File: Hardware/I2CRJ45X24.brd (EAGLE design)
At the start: 216 x 50 mm, 97 parts, among them IC1 MCP23017SO, IC2 MCP23017SO, IC3 MCP23017SO, IC4 MCP23017SO, IC5 MCP23017SO, IC6 MCP23017SO, J1 I2C-BREAKOUT, J2 I2C-BREAKOUT, J3 M01-PLAIN, J4 RJ45-X8, J5 RJ45-X8, J6 RJ45-X8

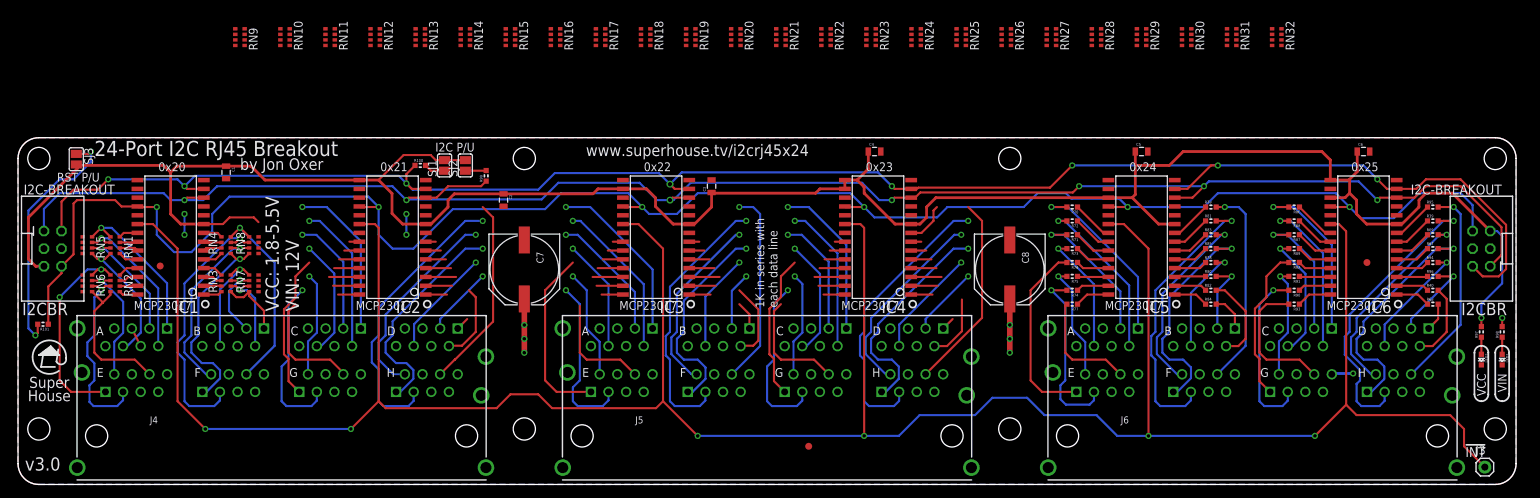
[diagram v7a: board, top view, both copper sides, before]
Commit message: Replace discrete resistors with resistor networks. Add hardware pull-ups to all input lines. Routing, ERC, and DRC for v3.0 release.
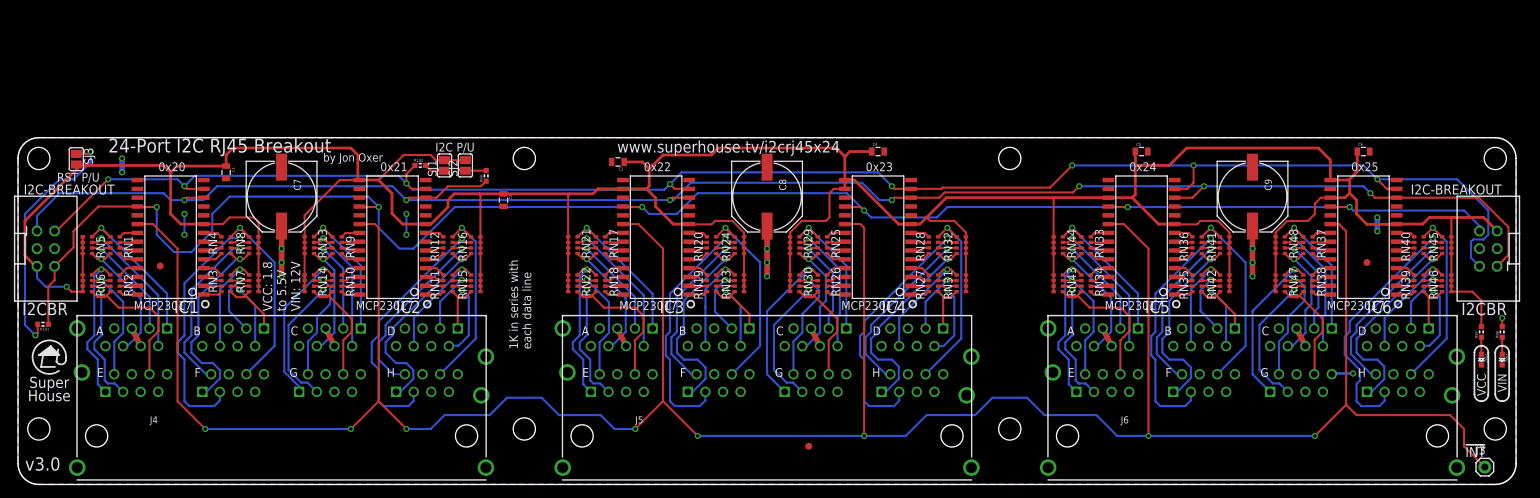
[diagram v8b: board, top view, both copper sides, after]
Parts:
- removed R39, R40, R67, R68, R69, R70, R71, R72, R73, R74, R75, R76, R77, R78, R79, R80, R81, R82, R83, R84, R85, R86, R87, R88, R89, R90, R91, R92, R93, R94, R95, R96: 1K, SuperHouse-DiscreteSemi:R0603
- added C9: 330uF 50V, SuperHouse-Capacitors:PANASONIC_G
- added RN33, RN34, RN35, RN36, RN37, RN38, RN39, RN40: 1K, SuperHouse-Resistors:CAY16
- added RN41, RN42, RN43, RN44, RN45, RN46, RN47, RN48: 10K, SuperHouse-Resistors:CAY16
- C1, C2, C3, C4, C5, C6: device SuperHouse-DiscreteSemi:C0805 -> SuperHouse-Capacitors:C0805
- C7, C8: device SuperHouse-DiscreteSemi:PANASONIC_G -> SuperHouse-Capacitors:PANASONIC_G
- R100, R101, R97, R98, R99: device SuperHouse-DiscreteSemi:R0603 -> SuperHouse-Resistors:R0603
- RN1, RN10, RN11, RN12, RN13, RN14, RN15, RN16, RN17, RN18, RN19, RN2, RN20, RN21, RN22, RN23, RN24, RN25, RN26, RN27, RN28, RN29, RN3, RN30, RN31, RN32, RN4, RN5, RN6, RN7, RN8, RN9: device SuperHouse-DiscreteSemi:CAY16 -> SuperHouse-Resistors:CAY16
- moved RN30 66.7 mm to (112.0, 29.0)
- moved RN29 58.3 mm to (112.0, 34.5)
- moved RN32 54.5 mm to (136.0, 34.5), turned to 270 degrees
- moved RN31 52.7 mm to (136.0, 29.0), turned to 270 degrees
- moved RN22 50.9 mm to (80.0, 29.0)
- moved RN26 44.3 mm to (116.0, 29.0)
- moved RN21 42.4 mm to (80.0, 34.5)
- moved RN14 42.0 mm to (42.0, 29.0)
- moved RN23 40.3 mm to (104.0, 29.0), turned to 270 degrees
- moved RN24 39.4 mm to (104.0, 34.5), turned to 270 degrees
- moved RN11 39.4 mm to (62.0, 29.0), turned to 270 degrees
- moved RN27 39.4 mm to (132.0, 29.0), turned to 270 degrees
- moved RN28 38.1 mm to (132.0, 34.5), turned to 270 degrees
- moved C7 36.5 mm to (38.0, 41.5)
- moved C8 36.5 mm to (108.0, 41.5)
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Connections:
- net 3A1: now also RN33.5, RN44.4; no longer R70.2
- net 3A2: now also RN33.6, RN44.3; no longer R72.2
- net 3A3: now also RN33.7, RN44.2; no longer R71.2
- net 3A6: now also RN33.8, RN44.1; no longer R73.2
- net 3B1: now also RN35.5, RN42.4; no longer R84.2
- net 3B2: now also RN35.6, RN42.3; no longer R82.2
- net 3B3: now also RN35.7, RN42.2; no longer R80.2
- net 3B6: now also RN35.8, RN42.1; no longer R78.2
- net 3C1: now also RN37.5, RN48.4; no longer R86.2
- net 3C2: now also RN37.6, RN48.3; no longer R88.2
- net 3C3: now also RN37.7, RN48.2; no longer R87.2
- net 3C6: now also RN37.8, RN48.1; no longer R89.2
- net 3D1: now also RN39.5, RN46.4; no longer R68.2
- net 3D2: now also RN39.6, RN46.3; no longer R40.2
- net 3D3: now also RN39.7, RN46.2; no longer R96.2
- net 3D6: now also RN39.8, RN46.1; no longer R94.2
- net 3E1: now also RN34.5, RN43.4; no longer R76.2
- net 3E2: now also RN34.6, RN43.3; no longer R75.2
- net 3E3: now also RN34.7, RN43.2; no longer R74.2
- net 3E6: now also RN34.8, RN43.1; no longer R77.2
- net 3F1: now also RN36.5, RN41.4; no longer R85.2
- net 3F2: now also RN36.6, RN41.3; no longer R83.2
- net 3F3: now also RN36.7, RN41.2; no longer R81.2
- net 3F6: now also RN36.8, RN41.1; no longer R79.2
- net 3G1: now also RN38.5, RN47.4; no longer R92.2
- net 3G2: now also RN38.6, RN47.3; no longer R91.2
- net 3G3: now also RN38.7, RN47.2; no longer R90.2
- net 3G6: now also RN38.8, RN47.1; no longer R93.2
- net 3H1: now also RN40.5, RN45.4; no longer R67.2
- net 3H2: now also RN40.6, RN45.3; no longer R69.2
- net 3H3: now also RN40.7, RN45.2; no longer R39.2
- net 3H6: now also RN40.8, RN45.1; no longer R95.2
- net GND: now also C9.-
- net GPA0-5: now also RN33.4; no longer R70.1
- net GPA0-6: now also RN37.4; no longer R86.1
- net GPA1-5: now also RN33.3; no longer R72.1
- net GPA1-6: now also RN37.3; no longer R88.1
- net GPA2-5: now also RN33.2; no longer R71.1
- net GPA2-6: now also RN37.2; no longer R87.1
- net GPA3-5: now also RN33.1; no longer R73.1
- net GPA3-6: now also RN37.1; no longer R89.1
- net GPA4-5: now also RN34.4; no longer R76.1
- net GPA4-6: now also RN38.4; no longer R92.1
- net GPA5-5: now also RN34.3; no longer R75.1
- net GPA5-6: now also RN38.3; no longer R91.1
- net GPA6-5: now also RN34.2; no longer R74.1
- net GPA6-6: now also RN38.2; no longer R90.1
- net GPA7-5: now also RN34.1; no longer R77.1
- net GPA7-6: now also RN38.1; no longer R93.1
- net GPB0-5: now also RN35.4; no longer R84.1
- net GPB0-6: now also RN39.4; no longer R68.1
- net GPB1-5: now also RN35.3; no longer R82.1
- net GPB1-6: now also RN39.3; no longer R40.1
- net GPB2-5: now also RN35.2; no longer R80.1
- net GPB2-6: now also RN39.2; no longer R96.1
- net GPB3-5: now also RN35.1; no longer R78.1
- net GPB3-6: now also RN39.1; no longer R94.1
- net GPB4-5: now also RN36.4; no longer R85.1
- net GPB4-6: now also RN40.4; no longer R67.1
- net GPB5-5: now also RN36.3; no longer R83.1
- net GPB5-6: now also RN40.3; no longer R69.1
- net GPB6-5: now also RN36.2; no longer R81.1
- net GPB6-6: now also RN40.2; no longer R39.1
- net GPB7-5: now also RN36.1; no longer R79.1
- net GPB7-6: now also RN40.1; no longer R95.1
- net VCC: now also RN41.5, RN41.6, RN41.7, RN41.8, RN42.5, RN42.6, RN42.7, RN42.8, RN43.5, RN43.6, RN43.7, RN43.8, RN44.5, RN44.6, RN44.7, RN44.8, RN45.5, RN45.6, RN45.7, RN45.8, RN46.5, RN46.6, RN46.7, RN46.8, RN47.5, RN47.6, RN47.7, RN47.8, RN48.5, RN48.6, RN48.7, RN48.8
- net VIN: now also C9.+
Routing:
- net VCC: track 335.7 -> 533.8 mm
- net VIN: track 19.6 -> 40.0 mm, vias 7 -> 10
- net !RESET: track 268.4 -> 256.2 mm
- net SDA: track 257.2 -> 249.4 mm
- net 1E1: track 30.3 -> 22.9 mm, vias 2 -> 1
- net 1E3: track 27.4 -> 20.5 mm
- net 1D1: track 1.93 -> 7.85 mm
- net 2D1: track 1.93 -> 7.85 mm
- net 3E3: track 25.7 -> 20.5 mm
- net 2B1: track 4.11 -> 9.18 mm
- net 2E6: track 16.0 -> 20.9 mm
- net 3E6: track 16.3 -> 21.0 mm
- net !INT: track 389.4 -> 394.0 mm, vias 6 -> 8
- net 3C1: track 25.0 -> 20.5 mm
- net 3E1: track 27.2 -> 22.9 mm, vias 0 -> 1
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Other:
- board text added: "VCC: 1.8 to 5.5V VIN: 12V"
- board text removed: "VCC: 1.8-5.5V VIN: 12V"
